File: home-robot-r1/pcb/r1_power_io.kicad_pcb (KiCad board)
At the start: 4 copper layers, 73.9 x 100 mm, 73 parts, among them J1 Battery in, J10 Bumper L, J11 Bumper R, J12 Arm button, J13 Motor toggle loop, J14 Spare I2C, J15 Spare GPIO, J2 Master rocker, J3 Jetson 5V, J4 Left motor, J5 Right motor, J6 Cliff 1, J7 Cliff 2, J8 Cliff 3, J9 Cliff 4, K1 G5LE-1 DC5, Q1 2N7002, Q2 2N7002, Q3 2N7002, Q4 2N7002, Q5 2N7002, U1A Pico left row, U1B Pico right row, U2 GY-521 MPU-6050, U3L DRV8874 left, VM/EN/PH row, U3P DRV8874 left, VIN/OUT row, U4L DRV8874 right, VM/EN/PH row, U4P DRV8874 right, VIN/OUT row, U5A Regulator in (P03 module), U5B Regulator out (P03 module)

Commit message: Sync: bay B12a connectors, B12b sim cleanups, task G bumper recovery
R1 from power-io-board 8bd8195:
- Battery, rocker and Jetson connectors that can't be swapped (J1 XT30, J2 VH, J3 Micro-Fit):
  board re-placed and re-routed, power check, fab files, CAD and harness updated.
- Final-review guide fixes (BRINGUP, ORDERING, pigtail lengths) and test cleanups.

Simulator from main 94d346d:
- Statistical scenario checks, IMU minors, C++/comment minors (B12b).
- Contact recovery with no straight trail behind the robot: re-planned back-off, slow creep
  over driven ground, then a 60 s cap and a stop message (task G).
- 2D house harness (tests/house2d), mapping analysis and the Unreal contact replay.
- docs/WORKFLOW.md: one task = one branch, one thread.

Co-Authored-By: Claude Opus 5.5 <noreply@anthropic.com>
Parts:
- J1: footprint Connector_JST:JST_VH_B2P-VH_1x02_P3.96mm_Vertical -> Connector_AMASS:AMASS_XT30UPB-M_1x02_P5.0mm_Vertical
- J3: footprint Connector_JST:JST_VH_B2P-VH_1x02_P3.96mm_Vertical -> Connector_Molex:Molex_Micro-Fit_3.0_43650-0200_1x02_P3.00mm_Horizontal
- moved J3 5.37 mm to (24.1, 90.5)
- moved J1 1.44 mm to (4.15, 73.0)
- moved K1 0.50 mm to (8.64, 96.5)
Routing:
- net ENC_RA_5V: track 122.7 -> 80.8 mm, vias 2 -> 3
- net SDA: track 156.7 -> 185.9 mm, vias 2 -> 4
- net ENC_LB_3V3: track 66.7 -> 46.0 mm
- net ENC_RB_5V: track 81.5 -> 99.4 mm, vias 1 -> 2
- net SCL: track 155.8 -> 170.5 mm, vias 1 -> 0
- net BUMP_L: track 60.3 -> 50.6 mm
- net SPARE1: track 64.9 -> 71.7 mm, vias 1 -> 5
- net BUMP_R: track 101.9 -> 96.8 mm, vias 0 -> 1
- net 3V3: track 211.2 -> 207.3 mm, vias 8 -> 7
- net ENC_RA_3V3: track 63.7 -> 67.6 mm
- net ENC_RB_3V3: track 39.4 -> 35.8 mm, vias 1 -> 2
- net DRV_FAULT: track 92.0 -> 89.8 mm
- net ENC_LA_3V3: track 39.5 -> 37.6 mm
- net ENC_LA_5V: track 33.0 -> 34.9 mm
- net LED2_A: track 35.8 -> 37.4 mm, vias 2 -> 4
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
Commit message: Board changes before fab: CS RC filters, DNP VSYS diode, ARM pull-up, 10k I2C pull-ups, 0.3 mm LP12 vias, JLCPCB DRC rules (LIO-226)
- CS filters: R24 / R25 (4.7k) + C4 / C5 (100 nF, LP12 GND vias) on new nets L_CS_ADC / R_CS_ADC
  (GP27 / GP28, RC 0.47 ms), placed beside the drivers' CS pins: both Pico columns are full at
  the silk-label pitch, so there is no legal 0805 spot by U1B.7 / U1B.9.
- D2: SS14 (SMA, DNP) from 5V to a new VSYS net at the Pico's pin 39 (U1B.2); VSYS left NC.
  The only legal SMA spot is the north end of DRV_R's interior.
- R26: 10k ARM pull-up at the foot of the U1A column, with a notch in the VBAT_SW F.Cu strip
  (4.93 mm left there, 7.6 A); its 3V3 end is a scripted pre-route.
- R19 / R20: 4.7k -> 10k (I2C bus ~1.05 k with the module pull-ups).
- SMD_PAD_VIA = (0.8, 0.3) for the SMD_GND_VIAS; net_via() takes the via position;
  stitching vias stay GND_VIA (0.8 / 0.4).
- DRC_RULES: JLCPCB 4-layer minimums (annular ring, plated / non-plated hole, hole to hole,
  copper to edge, silk line / text stroke, silk to mask), each checked against a deliberate
  violation; copper to edge stays at KiCad's 0.5 mm.
- Regenerated schematic, board, routing, fab package and board_cad.json; docs and tests updated.

Co-Authored-By: Claude Opus 5.5 <noreply@anthropic.com>
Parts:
- added C4: 100nF, Capacitor_SMD:C_0805_2012Metric, F.Cu at (53.0, 47.2)
- added C5: 100nF, Capacitor_SMD:C_0805_2012Metric, F.Cu at (42.2, 77.5)
- added D2: SS14, Diode_SMD:D_SMA, F.Cu at (40.5, 66.0)
- added R24: 4.7k, Resistor_SMD:R_0805_2012Metric, F.Cu at (51.5, 51.5)
- added R25: 4.7k, Resistor_SMD:R_0805_2012Metric, F.Cu at (43.0, 81.5)
- added R26: 10k, Resistor_SMD:R_0805_2012Metric, F.Cu at (13.2, 49.6)
- R19, R20: value 4.7k -> 10k
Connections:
- U1B pad 2: unconnected-(U1B-Pin_2-Pad2) -> VSYS
- U1B pad 7: R_CS -> R_CS_ADC
- U1B pad 9: L_CS -> L_CS_ADC
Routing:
- net VSYS: track 0.00 -> 92.1 mm, vias 0 -> 4
- net R_CS_ADC: track 0.00 -> 82.7 mm, vias 0 -> 1
- net R_CS: track 75.1 -> 3.82 mm
- net SCL: track 170.5 -> 221.3 mm, vias 0 -> 3
- net L_CS_ADC: track 0.00 -> 48.5 mm, vias 0 -> 1
- net LED3_A: track 3.01 -> 46.5 mm
- net 5V: track 112.7 -> 151.9 mm, vias 5 -> 7
- net L_CS: track 43.1 -> 6.53 mm
- net SDA: track 185.9 -> 156.8 mm, vias 4 -> 3
- net ENC_RA_5V: track 80.8 -> 93.9 mm, vias 3 -> 2
- net R_IN1: track 60.0 -> 48.3 mm
- net ENC_RB_3V3: track 35.8 -> 46.0 mm
- net ENC_LB_3V3: track 46.0 -> 54.3 mm
- net SPARE1: track 71.7 -> 63.9 mm, vias 5 -> 1
- net 3V3: track 207.3 -> 214.0 mm
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
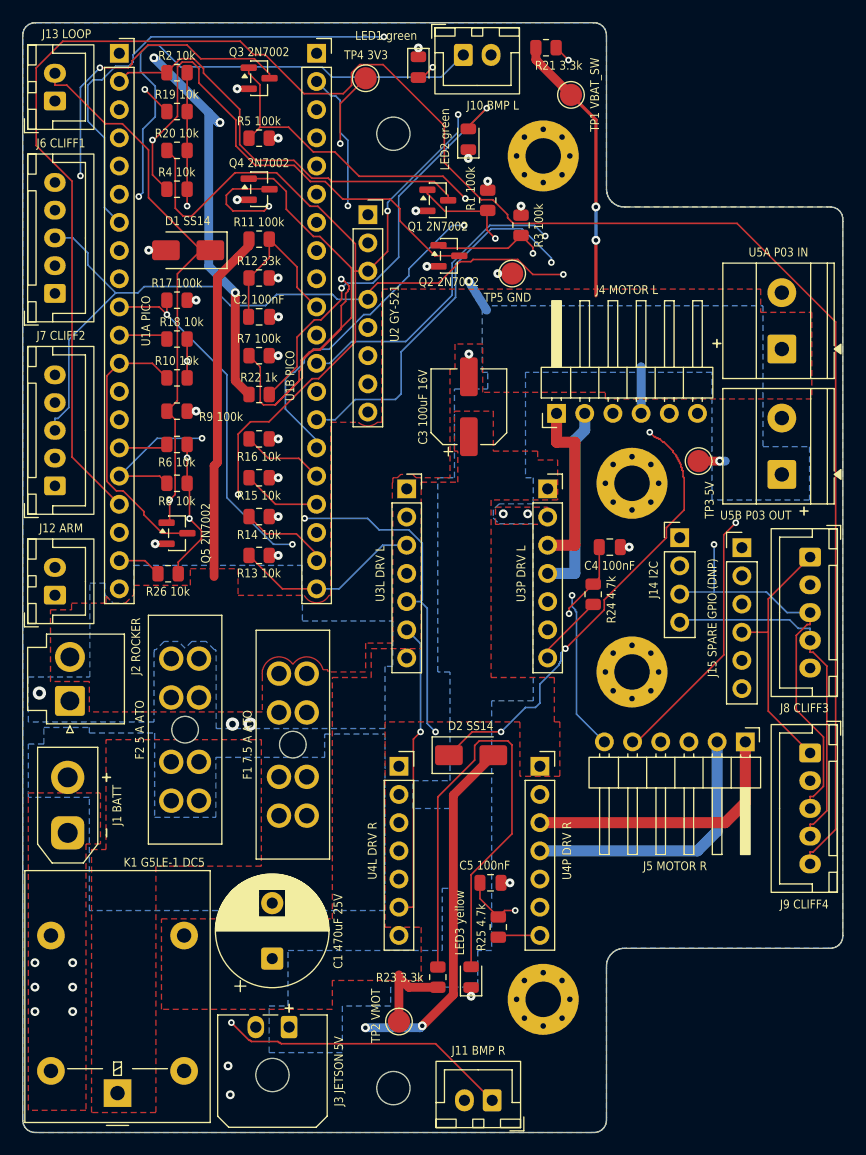
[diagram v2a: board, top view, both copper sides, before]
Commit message: Round-2 board: D2 5V tap via, scripted 0.25 mm VSYS, R_CS_ADC off the motor tracks, C4 / R24 labels, DRC rule severities, J1.1 ring cut rated as a stack (LIO-232, LIO-231)
- D2.2's 5V anode taps the 5V B.Cu strip through one pre-routed PowerTap via (41.6, 64.6), like TP3: the router's
  32 mm J3 -> D2 F.Cu chain is gone and LED3_A routes straight (46.5 -> 3.0 mm).
- VSYS is a scripted pre-route, 0.25 mm (0.27 A on 0.5 oz In2 at 10 degC vs PICO_VSYS_A 0.2 A; 0.15 mm carries 0.18 A):
  F.Cu -> In2 up DRV_L's interior -> B.Cu to U1B.2, 70.8 mm and 2 vias (was 92.1 mm, 4 vias, 38 mm of 0.15 mm In2;
  spanning tree 61.9 mm). Freerouting cannot leave D2's pocket (its DSN grows every via by VIA_GROW). VSYS joins
  TAP_NETS (source D2.K, load the Pico's VSYS pin), so power_check.track_loads covers it. The "0.15 mm carries
  0.25 A inner" comments (the 20 degC figure) now say 0.18 A.
- route.py keeps In2 copper MOTOR_SHADOW (0.5 mm) clear of the B.Cu Motor tracks (DSN keepout, stage F grid,
  quality count): R_CS_ADC now runs through the driver interiors, 4.72 mm from any motor track (it ran 11.9 mm
  under L_M2). A "1 mm west" leg was not legal: U3P.3 / U3P.4's 1.0 mm Motor clearance reaches u 49.33.
- C4's label 0.1 mm north (its own pads' silk gap allows no more) and R24's 0.4 mm south: 0.78 mm between them.
- The JLCPCB hole-to-hole, silk-to-mask, silk text stroke and silk line rules say (severity error).
- LIO-231: power_check.pin_ring_cut rates the layers' counted widths on their combined cross-section
  (copper.capacity_a): J1.1 was 6.71 A against 7.5 A (8.99 A summed). J1.1's F.Cu GND patch now reaches past K1.4
  and J1.1's south spoke (F2_OUT narrowed beside it, its trunk 7.12 A against 5 A): 7.84 A. The VMOT zones' 1.5 mm
  spokes lift K1.3's pad metric +2.5 -> +20.5 %; J2.1 stays +3.6 % (wider F1_OUT B.Cu spokes leave each F1.2 pad
  one spoke).
- ORDERING.md's verify list states the ring-cut outcome and the DRC severities; ktest_route checks the motor
  shadow, 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
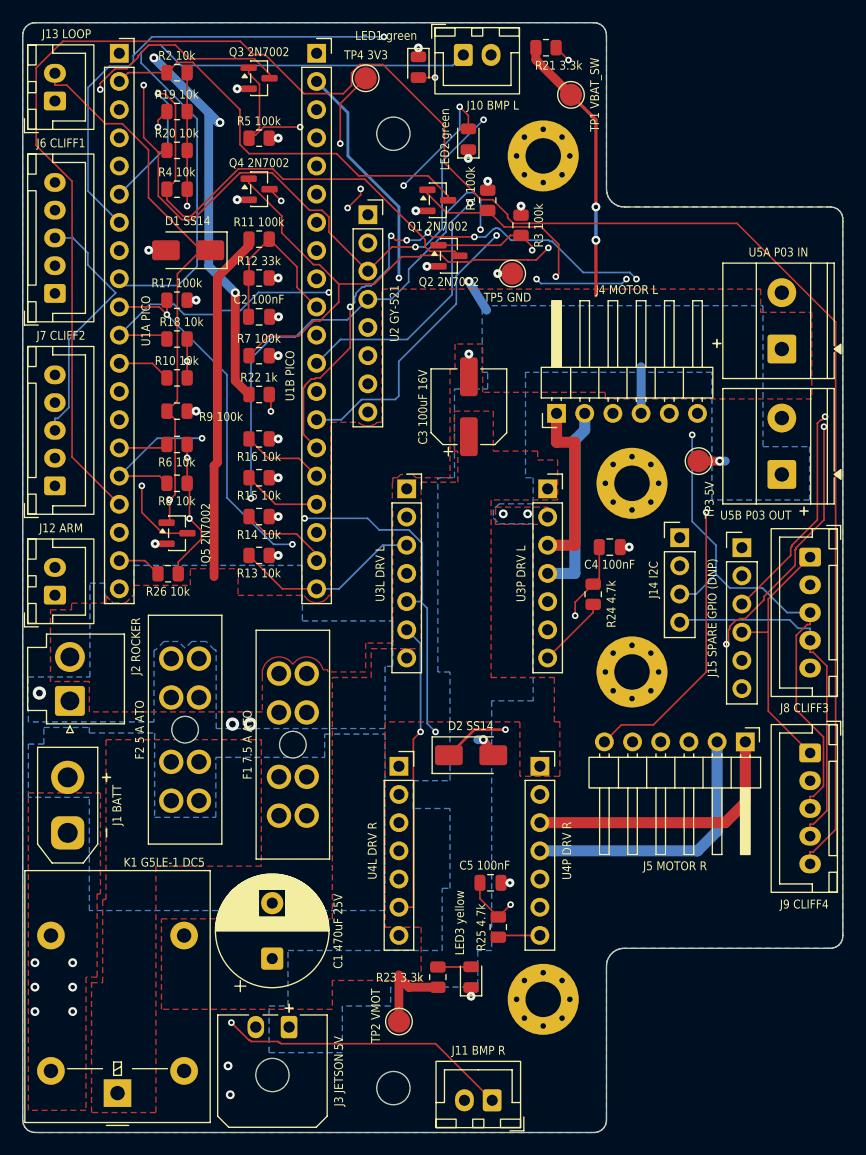
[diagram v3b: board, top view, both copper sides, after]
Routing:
- net LED3_A: track 46.5 -> 3.01 mm
- net 5V: track 151.9 -> 114.9 mm, vias 7 -> 6
- net SDA: track 156.8 -> 184.1 mm, vias 3 -> 4
- net VSYS: track 92.1 -> 70.8 mm, vias 4 -> 2
- net ENC_RA_5V: track 93.9 -> 110.7 mm, vias 2 -> 5
- net SPARE3: track 76.4 -> 90.8 mm, vias 1 -> 7
- net SCL: track 221.3 -> 209.6 mm
- net DRV_FAULT: track 86.7 -> 98.1 mm, vias 0 -> 1
- net L_CS_ADC: track 48.5 -> 55.5 mm
- net ENC_RB_3V3: track 46.0 -> 39.3 mm
- net R_CS_ADC: track 82.7 -> 76.0 mm
- net BUMP_L: track 53.6 -> 59.8 mm, vias 1 -> 0
- net LED2_A: track 38.2 -> 42.3 mm, vias 2 -> 5
- net SPARE1: track 63.9 -> 67.7 mm
- net XSHUT3: track 123.1 -> 120.1 mm
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
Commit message: Round-3 board: J2.1 / J1.2 / J2.2 / K1.1 / U5B.1 / J3.1 copper reworked, every trunk pin rated by its ring cut, lib_footprint_issues ignored, router tool checks, tooling fixes (LIO-236)
Zones (gen_power_zones, block regenerated; full pipeline re-run, routed clean):
- F1_OUT: B.Cu round J2.2 (the fill keeps its clearance), so J2.1's west pocket
  is live; an F.Cu helper west and south of J2.1 stitched to the B.Cu trunk by
  three vias (u 8.5 / 10.0 / 11.5, v 63.25; B.Cu lane to v 63.9 there, BAT+
  stepped to v 64.4 east of u 7.5); In2 copy also east of J2.1. J2.1's ring cut
  4.32 -> 10.33 A (round-3 max-flow 4.45 -> 8.76 A).
- BAT+: down to v 70.6 under J1.2, north edge kept for its mouth: 7.01 -> 7.92 A.
- VBAT_SW: F.Cu also west of J2.2: J2.2 6.41 -> 8.31 A (+10.8 %).
- F2_OUT: 1.5 mm spokes: K1.1 4.98 -> 5.75 A.
- 5V: U5B.1's box and the strip west of it to v 44.5, a block north-west of
  J3.1: U5B.1 4.31 -> 6.05 A, J3.1 4.91 -> 5.99 A.
- The new corners start at v 53.4, so R4's erosion leaves one piece.

Check (power_check): trunk_pin_ring rates every non-GND POWER_TRUNK pin by
pin_ring_cut out to the relief gap + 1.0 / 2.5 mm on a 0.05 mm whole-cell
raster (a fuse contact's pads joined), only layers that lead on to the trunk
(zone_check.pin_path_capacity 'live'); report section 3b; ktest_power asserts
>= (1 + LOW_MARGIN) x pad_current, cross-checks K1.3 and fails on a copy
without J2.1's F.Cu helper. raster_cut_mm blocked nothing past `outer` in rows
that miss the disc (fixed), and its cut ran free along its one ray: ring_cut_mm
takes the best of four ray directions. copper_raster clips to the ring. J1.1's
ring cut 7.84 -> 8.37 A (ORDERING.md updated; ktest_power pins the figure).

Tooling: make_schematic ignores lib_footprint_issues (DRC with an empty
KICAD_CONFIG_HOME 79 -> 0); route.router_tools exits unless the jar hash and
Java 25 match; tools._java keeps only JDK 25 and drops +build; track_loads
asserts its sources; MOTOR_SHADOW's pad hole documented as 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
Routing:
- net ENC_RB_5V: track 101.9 -> 126.3 mm, vias 2 -> 5
- net SDA: track 184.1 -> 207.6 mm, vias 4 -> 3
- net BUMP_L: track 59.8 -> 77.5 mm
- net LED1_A: track 15.8 -> 31.6 mm
- net ENC_LB_3V3: track 54.5 -> 43.6 mm
- net LED2_A: track 42.3 -> 53.0 mm, vias 5 -> 3
- net SCL: track 209.6 -> 199.8 mm, vias 3 -> 2
- net XSHUT3: track 120.1 -> 111.6 mm, vias 1 -> 6
- net ENC_RA_5V: track 110.7 -> 105.0 mm, vias 5 -> 3
- net ENC_RA_3V3: track 63.4 -> 58.5 mm, vias 1 -> 2
- net ENC_RB_3V3: track 39.3 -> 43.4 mm, vias 2 -> 1
- net SPARE1: track 67.7 -> 69.7 mm
- net ENC_LA_5V: track 33.8 -> 32.0 mm
- net ENC_LB_5V: track 31.3 -> 32.4 mm
- net SPARE2: track 69.3 -> 70.1 mm
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- added copper zone on F.Cu, net F1_OUT
